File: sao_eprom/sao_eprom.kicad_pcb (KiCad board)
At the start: 2 copper layers, 31 parts, among them U1 27C512, U2 74LS161, U3 74LS161, U4 74LS161, U5 74LS161, U6 PCAL6416APW, U7 24LC32, U8 74LS02, U9 AP3012

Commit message: I know how 2 power now
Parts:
- removed C9: C, Capacitor_THT:C_Disc_D3.0mm_W1.6mm_P2.50mm
- added C12: 1uF, Capacitor_THT:C_Disc_D3.0mm_W1.6mm_P2.50mm, F.Cu at (135.3, 109.8)
- added C13: 1uF, Capacitor_THT:C_Disc_D3.0mm_W1.6mm_P2.50mm, F.Cu at (140.3, 89.6)
- added C14: 1uF, Capacitor_THT:C_Disc_D3.0mm_W1.6mm_P2.50mm, F.Cu at (146.7, 109.8)
- added C15: 1uF, Capacitor_THT:C_Disc_D3.0mm_W1.6mm_P2.50mm, F.Cu at (151.8, 89.6)
- added D4: 1N5819, Diode_THT:D_DO-41_SOD81_P10.16mm_Horizontal, F.Cu at (140.3, 94.6)
- added D5: 1N5819, Diode_THT:D_DO-41_SOD81_P10.16mm_Horizontal, F.Cu at (151.8, 94.6)
- added L2: 10uH, Inductor_SMD:L_0805_2012Metric, F.Cu at (137.7, 104.1)
- added L3: 10uH, Inductor_SMD:L_0805_2012Metric, F.Cu at (149.1, 104.1)
- added Q1: RE1C002UNTCL, Package_TO_SOT_SMD:SOT-416, F.Cu at (132.7, 83.8)
- added Q2: RE1C002ZPTL, Package_TO_SOT_SMD:SOT-416, F.Cu at (135.9, 83.8)
- added Q3: RE1C002UNTCL, Package_TO_SOT_SMD:SOT-416, F.Cu at (139.1, 83.8)
- added Q4: RE1C002ZPTL, Package_TO_SOT_SMD:SOT-416, F.Cu at (142.3, 83.8)
- added Q5: RE1C002UNTCL, Package_TO_SOT_SMD:SOT-416, F.Cu at (145.4, 83.8)
- added Q6: RE1C002ZPTL, Package_TO_SOT_SMD:SOT-416, F.Cu at (148.6, 83.8)
- added Q7: RE1C002ZPTL, Package_TO_SOT_SMD:SOT-416, F.Cu at (151.8, 83.8)
- added R10: 100R, Resistor_THT:R_Axial_DIN0207_L6.3mm_D2.5mm_P7.62mm_Horizontal, F.Cu at (132.7, 71.8)
- added R11: 1K, Resistor_THT:R_Axial_DIN0207_L6.3mm_D2.5mm_P7.62mm_Horizontal, F.Cu at (135.9, 71.8)
- added R12: 100R, Resistor_THT:R_Axial_DIN0207_L6.3mm_D2.5mm_P7.62mm_Horizontal, F.Cu at (139.1, 71.8)
- added R13: 1K, Resistor_THT:R_Axial_DIN0207_L6.3mm_D2.5mm_P7.62mm_Horizontal, F.Cu at (142.2, 71.8)
- added R14: 100R, Resistor_THT:R_Axial_DIN0207_L6.3mm_D2.5mm_P7.62mm_Horizontal, F.Cu at (145.4, 71.8)
- added R15: 1K, Resistor_THT:R_Axial_DIN0207_L6.3mm_D2.5mm_P7.62mm_Horizontal, F.Cu at (148.6, 71.8)
- added R16: 100R, Resistor_THT:R_Axial_DIN0207_L6.3mm_D2.5mm_P7.62mm_Horizontal, F.Cu at (151.8, 71.8)
- added R17: 10K, Resistor_THT:R_Axial_DIN0207_L6.3mm_D2.5mm_P7.62mm_Horizontal, F.Cu at (94.5, 100.2)
- added R18: 10K, Resistor_THT:R_Axial_DIN0207_L6.3mm_D2.5mm_P7.62mm_Horizontal, F.Cu at (89.4, 100.2)
- added R6: R, Resistor_THT:R_Axial_DIN0207_L6.3mm_D2.5mm_P7.62mm_Horizontal, F.Cu at (137.2, 91.4)
- added R7: R, Resistor_THT:R_Axial_DIN0207_L6.3mm_D2.5mm_P7.62mm_Horizontal, F.Cu at (134.0, 99.1)
- added R8: R, Resistor_THT:R_Axial_DIN0207_L6.3mm_D2.5mm_P7.62mm_Horizontal, F.Cu at (148.6, 91.4)
- added R9: R, Resistor_THT:R_Axial_DIN0207_L6.3mm_D2.5mm_P7.62mm_Horizontal, F.Cu at (145.4, 99.1)
- added U10: AP3012, Package_TO_SOT_SMD:SOT-23-5, F.Cu at (145.9, 104.1)
- U8: value 74LS02 -> AP3012; footprint Package_DIP:DIP-14_W7.62mm -> Package_TO_SOT_SMD:SOT-23-5
- moved U8 77.3 mm to (123.0, 104.1)
- moved C6 67.2 mm to (104.8, 97.2)
- moved R1 66.1 mm to (103.4, 89.2)
- moved JP1 50.3 mm to (98.5, 78.3)
- moved U7 50.3 mm to (99.9, 73.3)
- moved SAO1 50.3 mm to (90.8, 72.4)
- moved U9 48.2 mm to (134.5, 104.1)
- moved C10 47.8 mm to (123.8, 109.8), turned to 90 degrees
- moved D3 46.9 mm to (128.9, 94.6), turned to -90 degrees
- moved C7 43.6 mm to (96.5, 84.5)
- moved U6 43.6 mm to (92.4, 90.2)
- moved L1 40.9 mm to (126.2, 104.1), turned to 90 degrees
- moved R5 40.6 mm to (122.6, 99.1), turned to 90 degrees
- moved C11 37.4 mm to (128.9, 89.6), turned to -90 degrees
- moved R4 35.8 mm to (125.7, 91.4), turned to -90 degrees
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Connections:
- D3 pad 2: Net-(L1-Pad2) -> Net-(D3-Pad2)
- L1 pad 2: Net-(L1-Pad2) -> Net-(D3-Pad2)
- R4 pad 2: Net-(U9-Pad3) -> Net-(R4-Pad2)
- R5 pad 1: Net-(U9-Pad3) -> Net-(R4-Pad2)
- U6 pad 15: /6V25EN -> /VPPEN
- U8 pad 1: Net-(U8-Pad1) -> Net-(D3-Pad2)
- U8 pad 2: /6V25EN -> GND
- U8 pad 3: /VDEN -> Net-(R4-Pad2)
- U8 pad 4: /12V5EN -> +3V3
- U8 pad 5: Net-(U8-Pad1) -> +3V3
- U9 pad 1: Net-(L1-Pad2) -> Net-(D4-Pad2)
- U9 pad 3: Net-(U9-Pad3) -> Net-(R6-Pad2)
- U9 pad 5: unconnected-(U9-Pad5) -> +3V3
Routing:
- net GND: track 192.8 -> 287.6 mm
- net +3V3: track 0.00 -> 41.9 mm
- net /12V5: track 0.00 -> 28.2 mm, vias 0 -> 2
- net /6V25: track 0.00 -> 20.5 mm, vias 0 -> 1
- net Net-(R8-Pad2): track 0.00 -> 11.7 mm
- net Net-(R4-Pad2): track 0.00 -> 11.7 mm
- net Net-(R6-Pad2): track 0.00 -> 11.7 mm
- net Net-(D4-Pad2): track 0.00 -> 8.17 mm
- net Net-(D3-Pad2): track 0.00 -> 8.17 mm
- net Net-(D5-Pad2): track 0.00 -> 8.17 mm
- net Net-(Q3-Pad3): track 0.00 -> 6.31 mm
- net Net-(Q5-Pad3): track 0.00 -> 6.30 mm
- net Net-(Q1-Pad3): track 0.00 -> 6.30 mm
- net +5V: track 141.7 -> 147.7 mm
- net VMEM: track 22.7 -> 27.4 mm, vias 0 -> 2
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
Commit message: Finish the first design revision
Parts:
- removed SAO1: Conn_2x3, Connector_PinHeader_2.54mm:PinHeader_2x03_P2.54mm_Vertical
- added G1: LOGO, LOGO, F.Cu at (160.7, 48.9)
- added H1: MountingHole_Pad, MountingHole:MountingHole_3mm_Pad_Via, F.Cu at (146.7, 110.5)
- added H2: MountingHole_Pad, MountingHole:MountingHole_3mm_Pad_Via, F.Cu at (146.7, 42.5)
- added H3: MountingHole_Pad, MountingHole:MountingHole_3mm_Pad_Via, F.Cu at (225.4, 110.5)
- added H4: MountingHole_Pad, MountingHole:MountingHole_3mm_Pad_Via, F.Cu at (225.4, 42.5)
- added J1: Conn_02x03_Odd_Even, Connector_PinHeader_2.54mm:PinHeader_2x03_P2.54mm_Vertical, F.Cu at (147.3, 49.5)
- moved Q2 77.3 mm to (209.6, 60.3)
- moved Q7 77.3 mm to (225.4, 60.3)
- moved R11 77.3 mm to (209.6, 48.3)
- moved R16 77.3 mm to (225.4, 48.3)
- moved Q1 77.3 mm to (206.4, 60.3)
- moved Q3 77.3 mm to (212.7, 60.3)
- moved Q4 77.3 mm to (215.9, 60.3)
- moved Q5 77.3 mm to (219.1, 60.3)
- moved Q6 77.3 mm to (222.2, 60.3)
- moved R10 77.3 mm to (206.4, 48.3)
- moved R12 77.3 mm to (212.7, 48.3)
- moved R13 77.3 mm to (215.9, 48.3)
- moved R14 77.3 mm to (219.1, 48.3)
- moved R15 77.3 mm to (222.2, 48.3)
- moved R1 75.0 mm to (174.5, 65.4), turned to 180 degrees
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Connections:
- C7 pad 1: +3V3 -> +5V
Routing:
- net /VPPEN: track 0.00 -> 127.2 mm, vias 0 -> 1
- net +3V3: track 41.9 -> 165.5 mm, vias 0 -> 4
- net /VDEN: track 0.00 -> 113.0 mm, vias 0 -> 2
- net +5V: track 147.7 -> 251.7 mm, vias 0 -> 5
- net /EPROM interface/~{OE}: track 0.00 -> 103.8 mm, vias 0 -> 3
- net GND: track 287.6 -> 386.4 mm, vias 5 -> 14
- net /EPROM interface/CLK: track 52.9 -> 108.8 mm, vias 0 -> 2
- net /EPROM interface/~{CE}: track 73.4 -> 126.2 mm, vias 0 -> 2
- net /SDA: track 0.00 -> 50.2 mm
- net /12V5: track 28.2 -> 77.1 mm
- net /SCL: track 0.00 -> 47.9 mm
- net Net-(R1-Pad2): track 0.00 -> 44.5 mm, vias 0 -> 1
- net /6V25: track 20.5 -> 64.9 mm
- net /EPROM interface/DB0: track 58.2 -> 100.6 mm, vias 0 -> 1
- net /EPROM interface/DB1: track 59.5 -> 99.3 mm, vias 0 -> 1
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- added copper zone on B.Cu, net GND
- added copper zone on F.Cu, net GND
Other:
- board outline added: 85.1 x 74.3 mm
- board text added: "Designed for read/write AM27C512, reads most 27C* EPROMS"
- board text added: "EPROM Reader/Writer v1.0 Julian Scheffers 23 April 2023"
- board text added: "Hardware support: RO *27C64 RO *27C128 RO *27C256 RW *27C512"

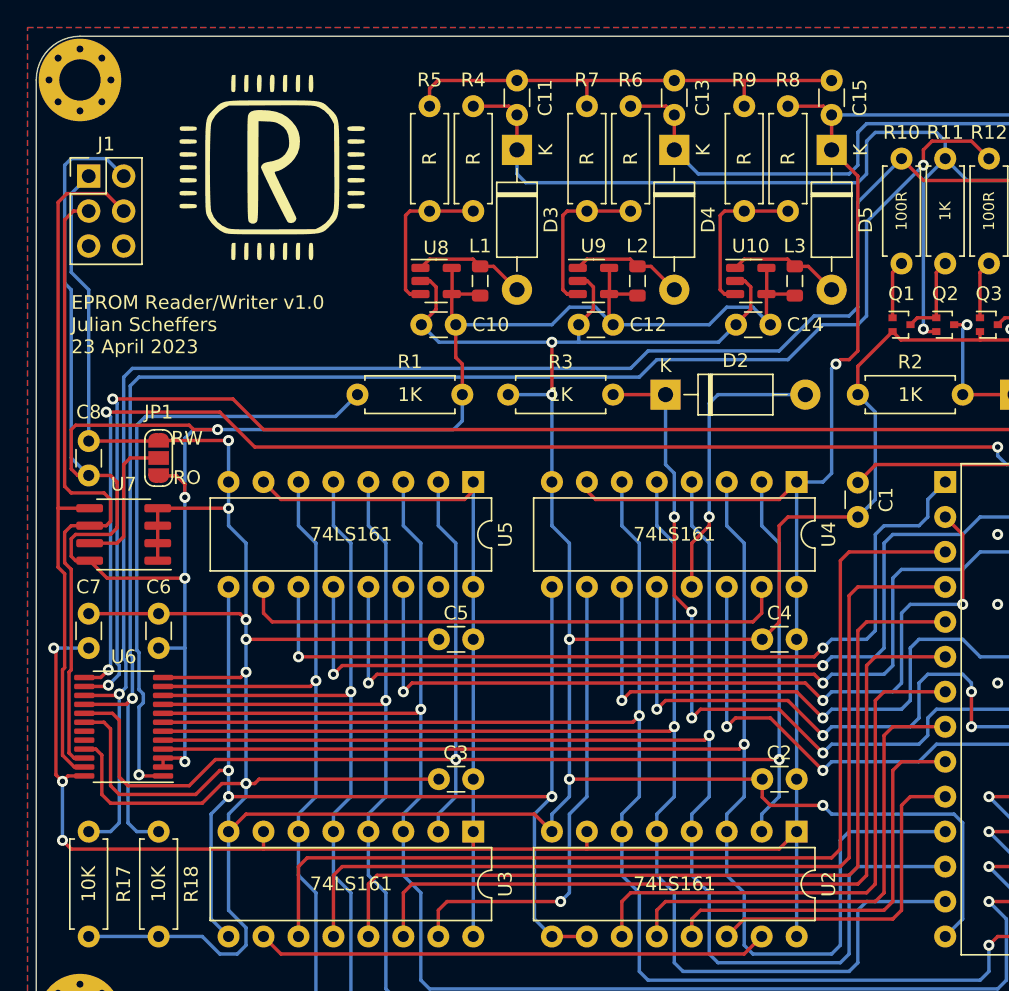
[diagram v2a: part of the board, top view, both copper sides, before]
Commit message: Do some resistor calculations
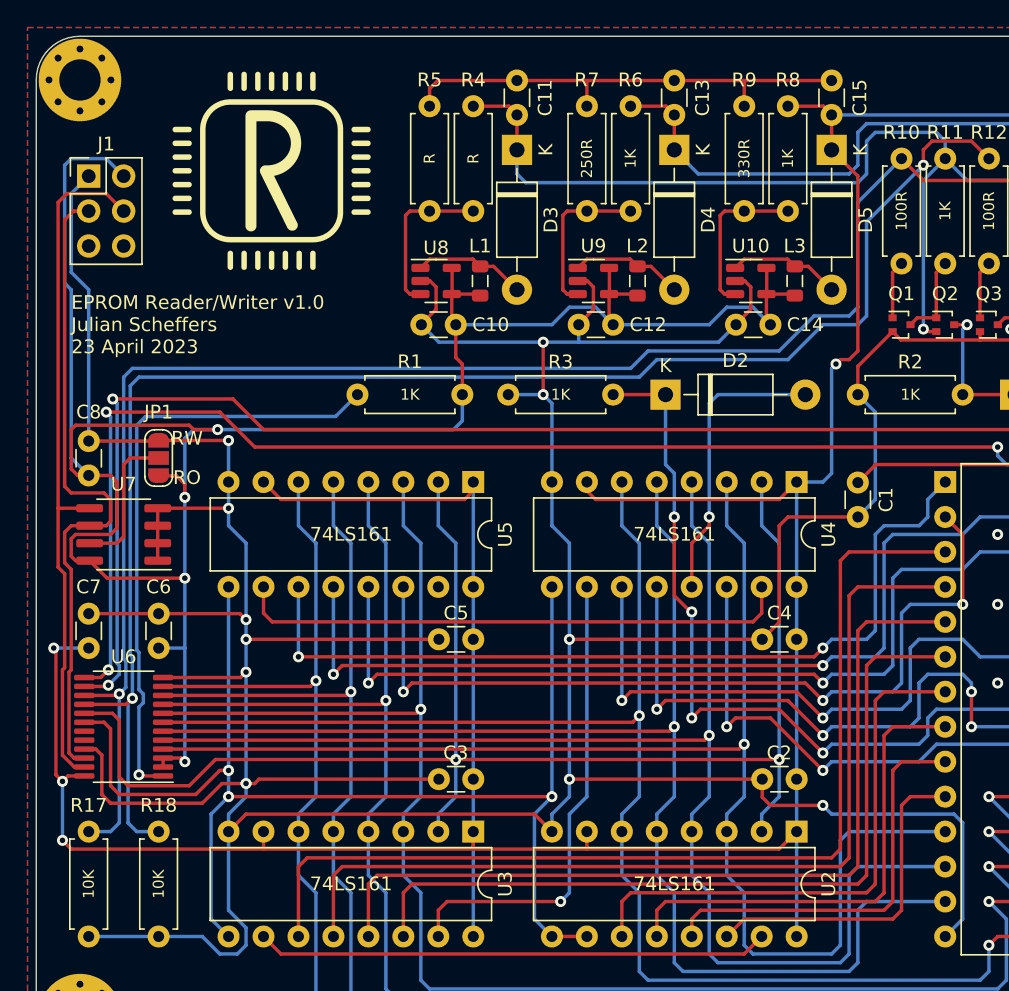
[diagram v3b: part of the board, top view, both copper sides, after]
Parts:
- removed G1: LOGO, LOGO
- R6, R8: value R -> 1K
- R7: value R -> 250R
- R9: value R -> 330R
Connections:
- net /12V5 renamed /12V75

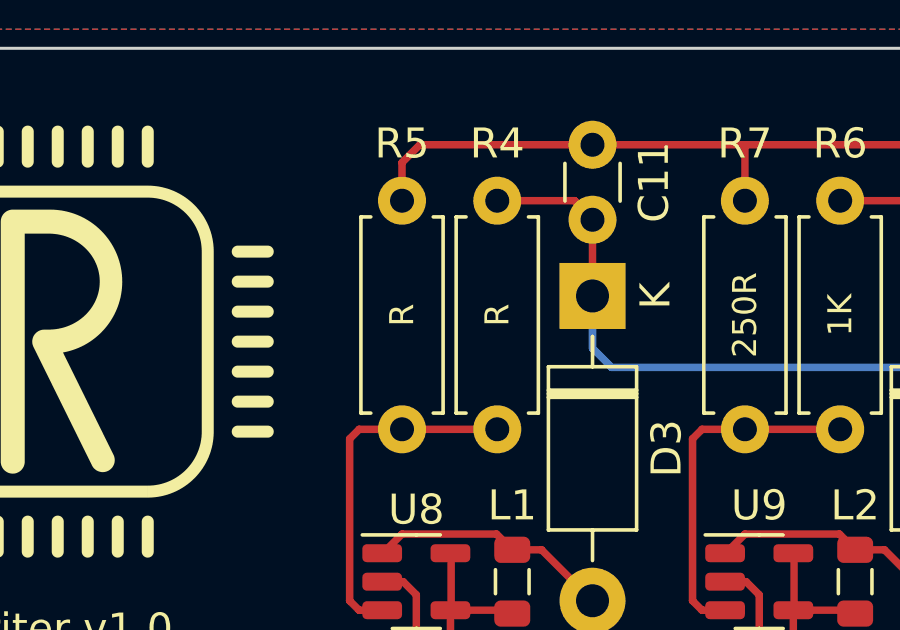
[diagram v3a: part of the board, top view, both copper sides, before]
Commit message: Choose final resistor values
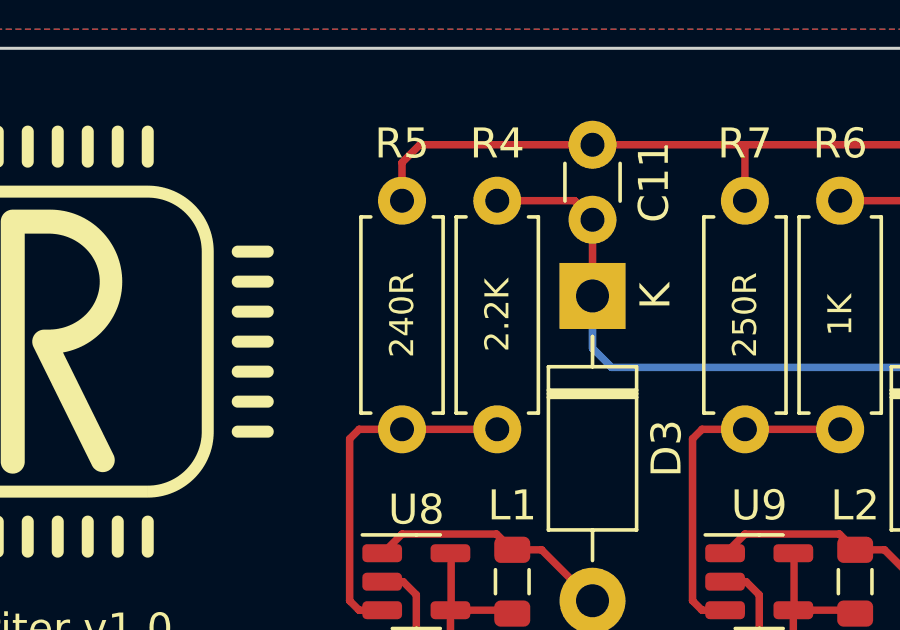
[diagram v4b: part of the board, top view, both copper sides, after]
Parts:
- R4: value R -> 2.2K
- R5: value R -> 240R
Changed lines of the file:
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@@
       (effects (font (size 1 1) (thickness 0.15)))
     )
-    (fp_text value "R" (at 3.81 0 90) (layer "F.SilkS")
+    (fp_text value "240R" (at 3.81 0 90) (layer "F.SilkS")
       (effects (font (size 0.8 0.8) (thickness 0.15)))
     )
@@
       (effects (font (size 1 1) (thickness 0.15)))
     )
-    (fp_text value "R" (at 3.81 0 90) (layer "F.SilkS")
+    (fp_text value "2.2K" (at 3.81 0 90) (layer "F.SilkS")
       (effects (font (size 0.8 0.8) (thickness 0.15)))
     )
@@
     (connect_pads (clearance 0))
     (min_thickness 0.254)
-    (keepout (tracks allowed) (vias allowed) (pads allowed) (copperpour not_allowed) (footprints allowed))
+    (keepout (tracks allowed) (vias allowed) (pads allowed ) (copperpour not_allowed) (footprints allowed))
     (fill (thermal_gap 0.508) (thermal_bridge_width 0.508))
     (polygon
